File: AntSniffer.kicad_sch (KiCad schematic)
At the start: 4 parts, among them CN1 X2026WRS-2X09D-LPSW, CN2 X2026WRS-2X09D-LPSW, J1 Conn_01x10_MountingPin

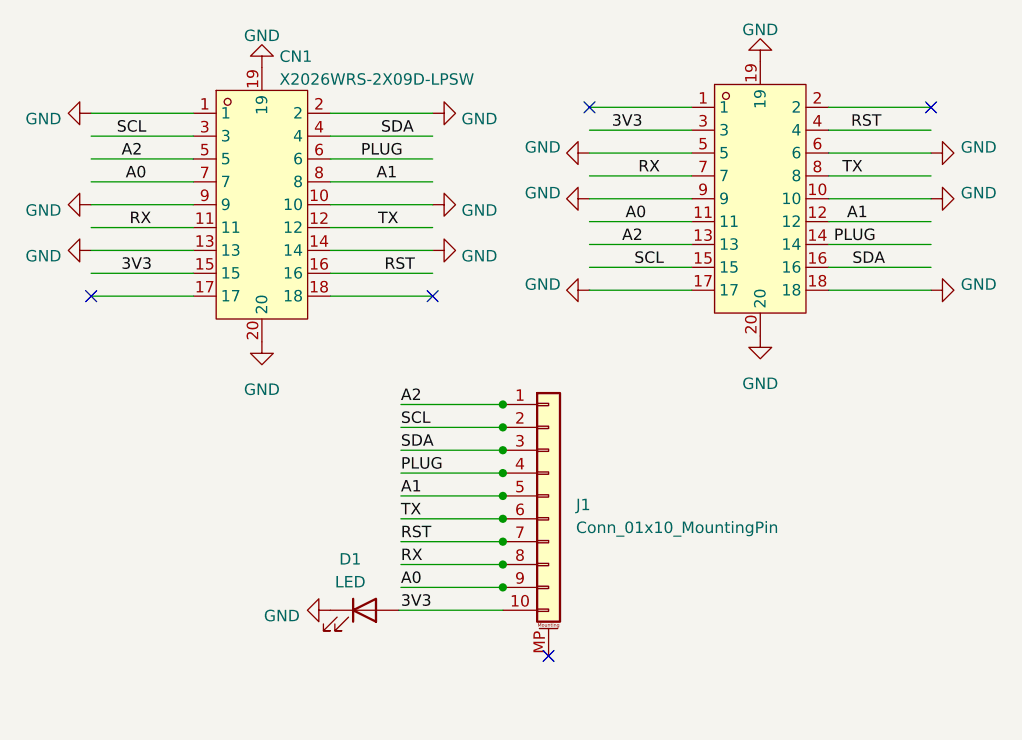
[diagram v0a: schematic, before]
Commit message: switched to two layer board. added GND pin
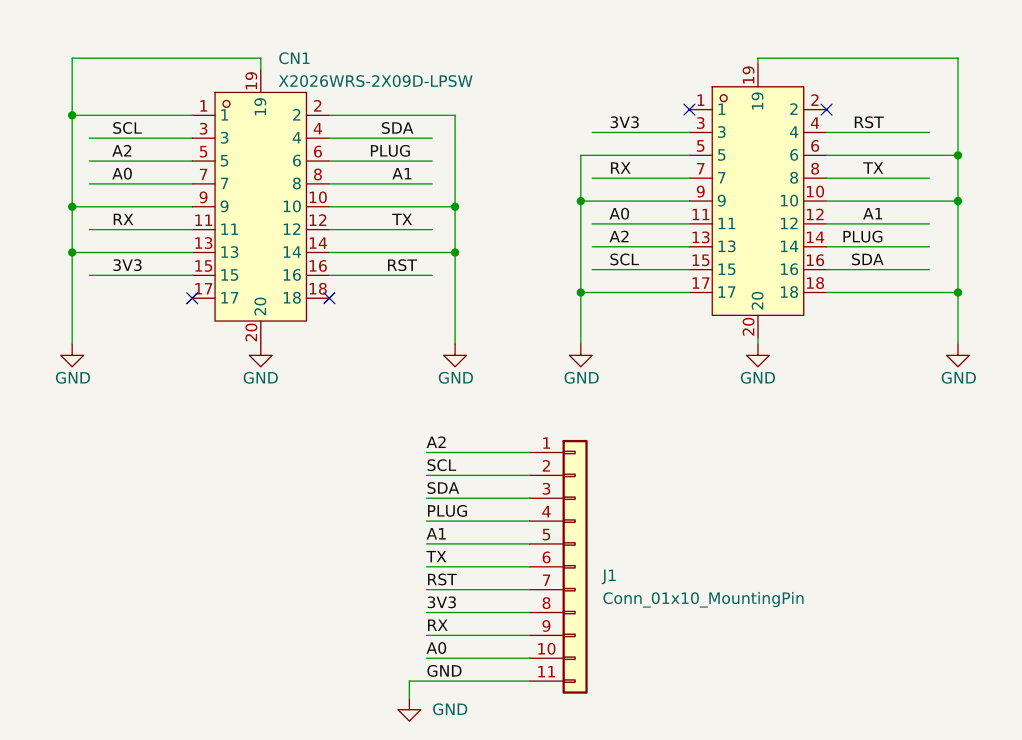
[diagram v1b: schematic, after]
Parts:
- removed D1: LED, LED_SMD:LED_0603_1608Metric, symbol Device:LED
- J1: footprint Connector_PinHeader_2.54mm:PinHeader_1x10_P2.54mm_Vertical -> Connector_PinHeader_2.54mm:PinHeader_1x11_P2.54mm_Vertical; symbol Connector_Generic_MountingPin:Conn_01x10_MountingPin -> Connector_Generic:Conn_01x11
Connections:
- net 3V3: now also J1.8 (Pin_8); no longer J1.10 (Pin_10)
- net A0: now also J1.10 (Pin_10); no longer J1.9 (Pin_9)
- net GND: now also J1.11 (Pin_11)
- net RX: now also J1.9 (Pin_9); no longer J1.8 (Pin_8)
- no-connect marks 5 -> 4

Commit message: moved libraries local, updated render, generated BOM and manufacturing files
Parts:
- CN1, CN2: footprint EASYEDA2KICAD:CONN-SMD_X2026WRS-2X09D-LPSW -> antsniffer:CONN-SMD_X2026WRS-2X09D-LPSW; symbol x2026:X2026WRS-2X09D-LPSW -> antsniffer:X2026WRS-2X09D-LPSW
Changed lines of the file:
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@@
   (title_block
     (title "Antsniffer")
-    (date "2023-11-04")
-    (rev "1.0")
+    (date "2023-11-06")
+    (rev "2.0")
   )
   (junction (at 110.49 52.705) (diameter 0) (color 0 0 0 0)
@@
     )
   )
-  (symbol (lib_id "x2026:X2026WRS-2X09D-LPSW") (at 74.93 43.18 0) (unit 1)
-    (in_bom yes) (on_board yes) (dnp no) (fields_autoplaced)
-    (property "Reference" "CN1" (at 76.8859 26.7208 0)
+  (symbol (lib_id "antsniffer:X2026WRS-2X09D-LPSW") (at 74.93 43.18 0) (unit 1)
+    (in_bom yes) (on_board yes) (dnp no)
+    (property "Reference" "CN1" (at 76.2 29.21 0)
       (effects (font (size 1.27 1.27)) (justify left))
     )
-    (property "Value" "X2026WRS-2X09D-LPSW" (at 76.8859 29.2608 0)
-      (effects (font (size 1.27 1.27)) (justify left))
-    )
-    (property "Footprint" "EASYEDA2KICAD:CONN-SMD_X2026WRS-2X09D-LPSW" (at 74.93 66.04 0)
+    (property "Value" "X2026WRS-2X09D-LPSW" (at 77.1241 27.94 0)
+      (effects (font (size 1.27 1.27)) (justify left) hide)
+    )
+    (property "Footprint" "antsniffer:CONN-SMD_X2026WRS-2X09D-LPSW" (at 74.93 66.04 0)
       (effects (font (size 1.27 1.27)) hide)
     )
@@
     )
   )
-  (symbol (lib_id "x2026:X2026WRS-2X09D-LPSW") (at 130.175 42.545 0) (unit 1)
-    (in_bom yes) (on_board yes) (dnp no) (fields_autoplaced)
-    (property "Reference" "CN2" (at 132.1309 26.416 0)
-      (effects (font (size 1.27 1.27)) (justify left) hide)
+  (symbol (lib_id "antsniffer:X2026WRS-2X09D-LPSW") (at 130.175 42.545 0) (unit 1)
+    (in_bom yes) (on_board yes) (dnp no)
+    (property "Reference" "CN2" (at 131.445 28.575 0)
+      (effects (font (size 1.27 1.27)) (justify left))
     )
     (property "Value" "X2026WRS-2X09D-LPSW" (at 132.1309 28.956 0)
       (effects (font (size 1.27 1.27)) (justify left) hide)
     )
-    (property "Footprint" "EASYEDA2KICAD:CONN-SMD_X2026WRS-2X09D-LPSW" (at 130.175 65.405 0)
+    (property "Footprint" "antsniffer:CONN-SMD_X2026WRS-2X09D-LPSW" (at 130.175 65.405 0)
       (effects (font (size 1.27 1.27)) hide)
     )
